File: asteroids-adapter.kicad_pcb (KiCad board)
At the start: 2 copper layers, 69 x 90.3 mm, 16 parts, among them J1 Asteroids PCB connector, J2 Asteroids harness connector, U1 TL074

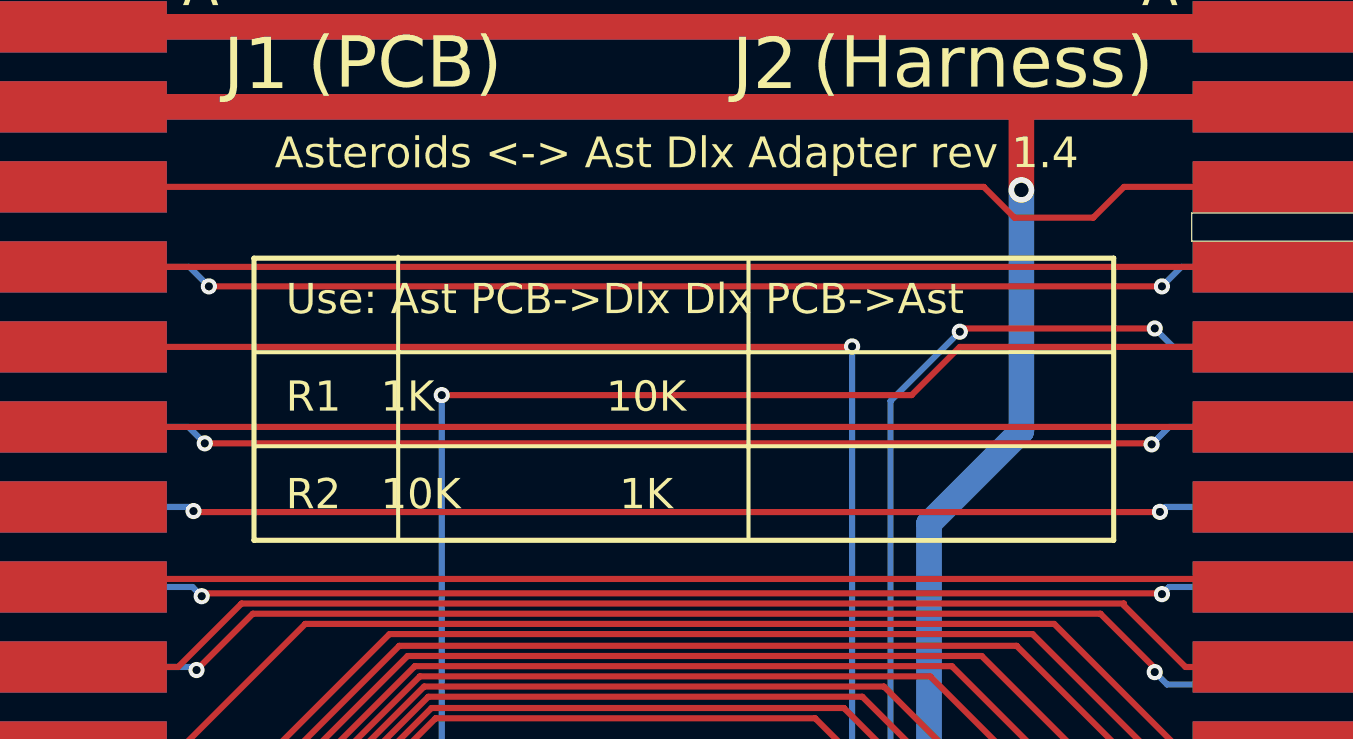
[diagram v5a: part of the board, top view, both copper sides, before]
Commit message: Rearranged config silk screen table
- easier to understand row format.
- white boxes to mark selected configuration.
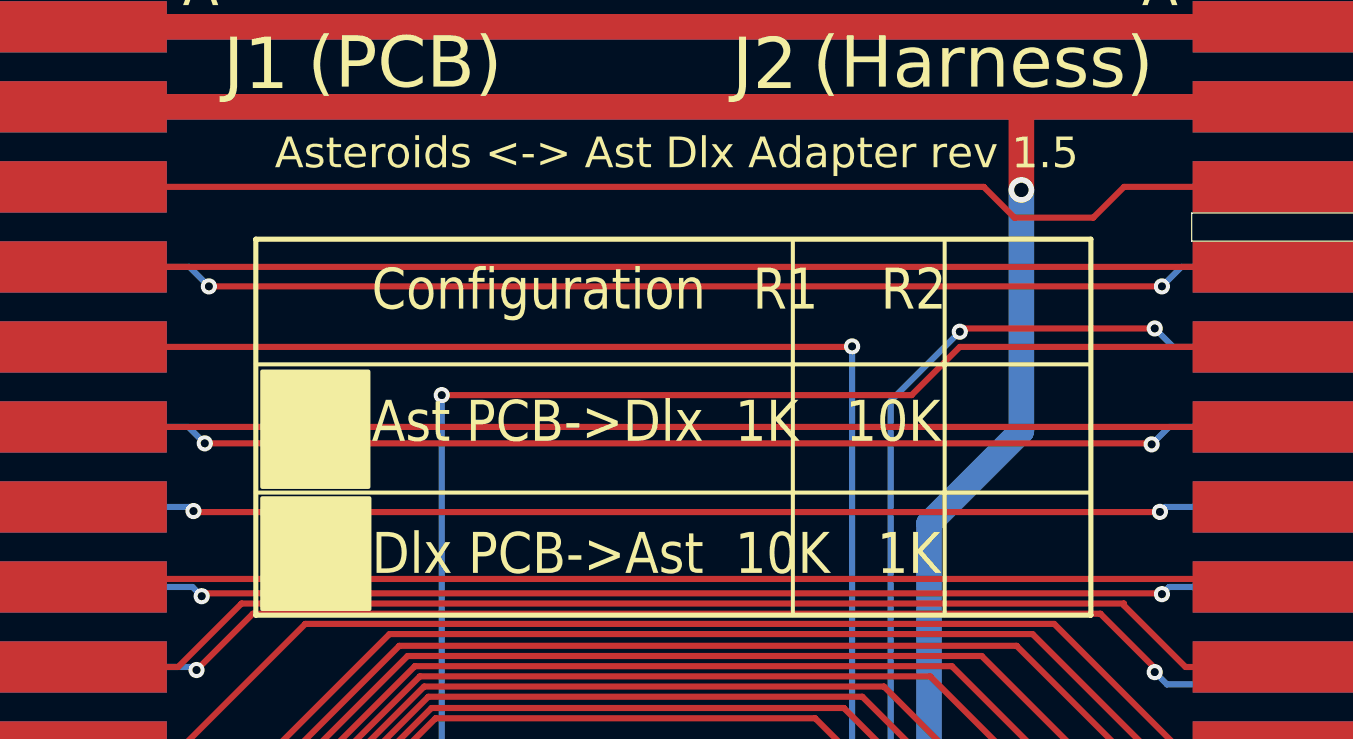
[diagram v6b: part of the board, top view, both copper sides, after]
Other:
- board text added: "Asteroids <-> Ast Dlx Adapter rev 1.5"
- board text added: "Configuration R1 R2 Ast PCB->Dlx 1K 10K Dlx PCB->Ast 10K 1K"
- board text removed: "Asteroids <-> Ast Dlx Adapter rev 1.4"
- board text removed: "Use: Ast PCB->Dlx Dlx PCB->Ast R1 1K 10K R2 10K 1K"
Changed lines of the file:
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@@
   (title_block
     (title "Asteroids to Asteroids Deluxe Adapter")
-    (date "2022-03-08")
-    (rev "1.4")
+    (date "2022-03-09")
+    (rev "1.5")
   )
   (layers
@@
     )
   )
-  (gr_line (start 145.2372 67.3862) (end 145.2372 81.3562) (layer "F.SilkS") (width 0.2))
-  (gr_line (start 120.7516 76.699532) (end 163.322 76.699532) (layer "F.SilkS") (width 0.2))
-  (gr_line (start 127.889 67.31) (end 127.889 81.28) (layer "F.SilkS") (width 0.2))
-  (gr_line (start 120.7516 72.042866) (end 163.322 72.042866) (layer "F.SilkS") (width 0.2))
-  (gr_rect (start 120.7516 67.3862) (end 163.322 81.3562) (layer "F.SilkS") (width 0.254) (fill none))
+  (gr_line (start 154.9527 66.4464) (end 154.9527 85.0646) (layer "F.SilkS") (width 0.2))
+  (gr_rect (start 121.158 78.7146) (end 126.4158 72.9996) (layer "F.SilkS") (width 0.2) (fill solid))
+  (gr_line (start 120.8405 78.994) (end 162.1917 78.994) (layer "F.SilkS") (width 0.2))
+  (gr_line (start 147.4343 66.4464) (end 147.4343 85.0646) (layer "F.SilkS") (width 0.2))
+  (gr_line (start 120.8405 72.644) (end 162.1917 72.644) (layer "F.SilkS") (width 0.2))
+  (gr_rect (start 121.158 84.7598) (end 126.4666 79.2734) (layer "F.SilkS") (width 0.2) (fill solid))
+  (gr_rect (start 120.8405 66.4464) (end 162.1917 85.0646) (layer "F.SilkS") (width 0.254) (fill none))
   (gr_poly
     (pts
@@
     (effects (font (size 1.905 1.905) (thickness 0.3)) (justify mirror))
   )
-  (gr_text "Asteroids <-> Ast Dlx Adapter rev 1.4" (at 141.6812 62.1792) (layer "F.SilkS")
+  (gr_text "Asteroids <-> Ast Dlx Adapter rev 1.5\n" (at 141.6812 62.1792) (layer "F.SilkS")
     (effects (font (size 1.524 1.524) (thickness 0.3)))
   )
@@
     (effects (font (size 1.905 1.905) (thickness 0.3)) (justify mirror))
   )
-  (gr_text "Use: Ast PCB->Dlx Dlx PCB->Ast\n\nR1   1K             10K\n \nR2   10K            1K" (at 122.3264 74.2442) (layer "F.SilkS")
-    (effects (font (size 1.5 1.5) (thickness 0.3)) (justify left))
+  (gr_text "Configuration   R1    R2\n\nAst PCB->Dlx  1K   10K\n\nDlx PCB->Ast  10K   1K" (at 126.5809 75.4888) (layer "F.SilkS")
+    (effects (font (size 2.032 1.778) (thickness 0.3048)) (justify left))
   )
   (segment (start 148.336 108.458) (end 138.43 108.458) (width 0.508) (layer "F.Cu") (net 1))
@@
     )
   )
-  (group "" (id 119bed15-d87d-4a81-bafe-b71226471a26)
+  (group "" (id 783ddcea-5963-4365-9c5b-b3f14c41286e)
     (members
       26e47b96-e9a5-48fa-bb2f-09aeb167fcf1
+      35b0aa54-b7ab-4dce-b263-08a43437121f
       644be4a6-1e55-414d-a68c-a545e48e63e7
       90662c63-00a8-414d-b291-156d808a5167
       d71882e2-ac98-42c6-8f8a-dd4c82632084
+      e6125ca4-8c3c-48b2-807d-2c2fe81d8bc7
       e79214a2-52a4-44d6-8e2b-47ef01e1d5a4
       eacccbd5-168c-4a45-b441-88af3d877755

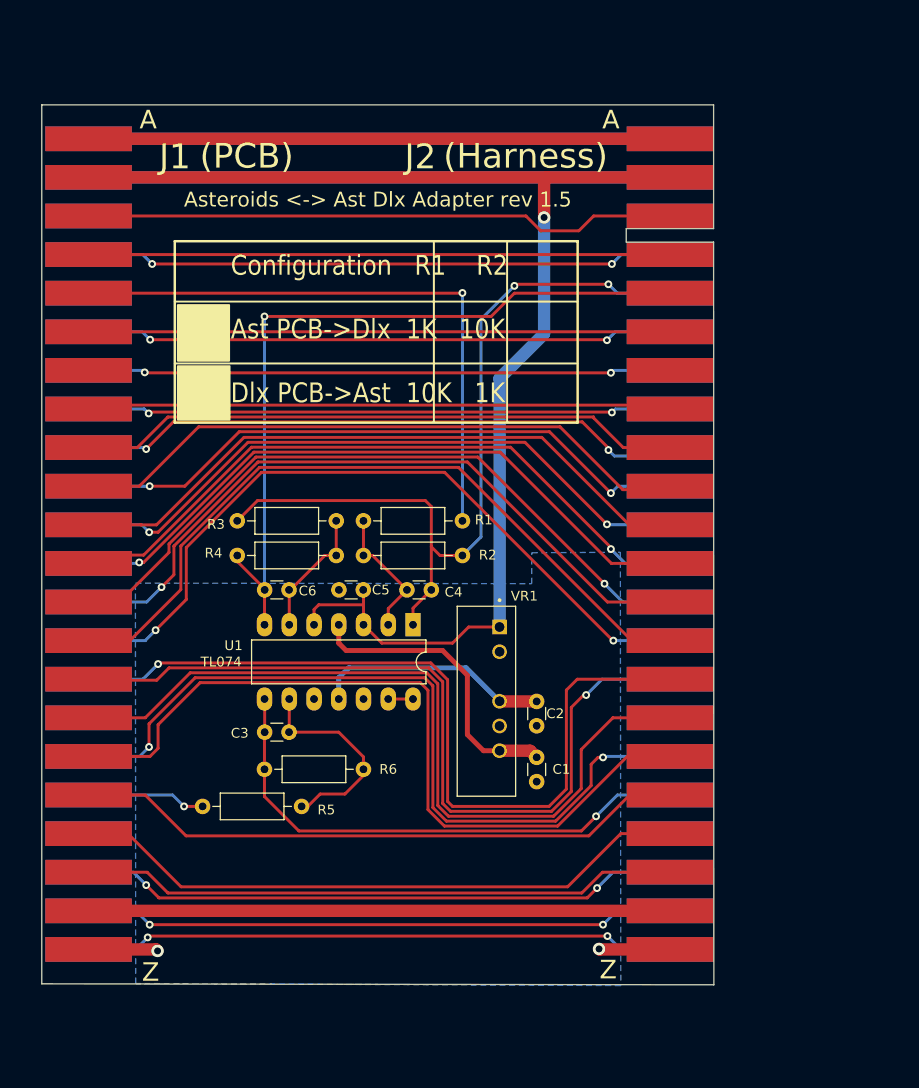
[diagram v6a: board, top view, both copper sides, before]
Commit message: Swith to PCB-mount edge connector
This is easier to assemble and provides a more reliable connection, due
to reduced likelyhood of distorting the edge connector position.
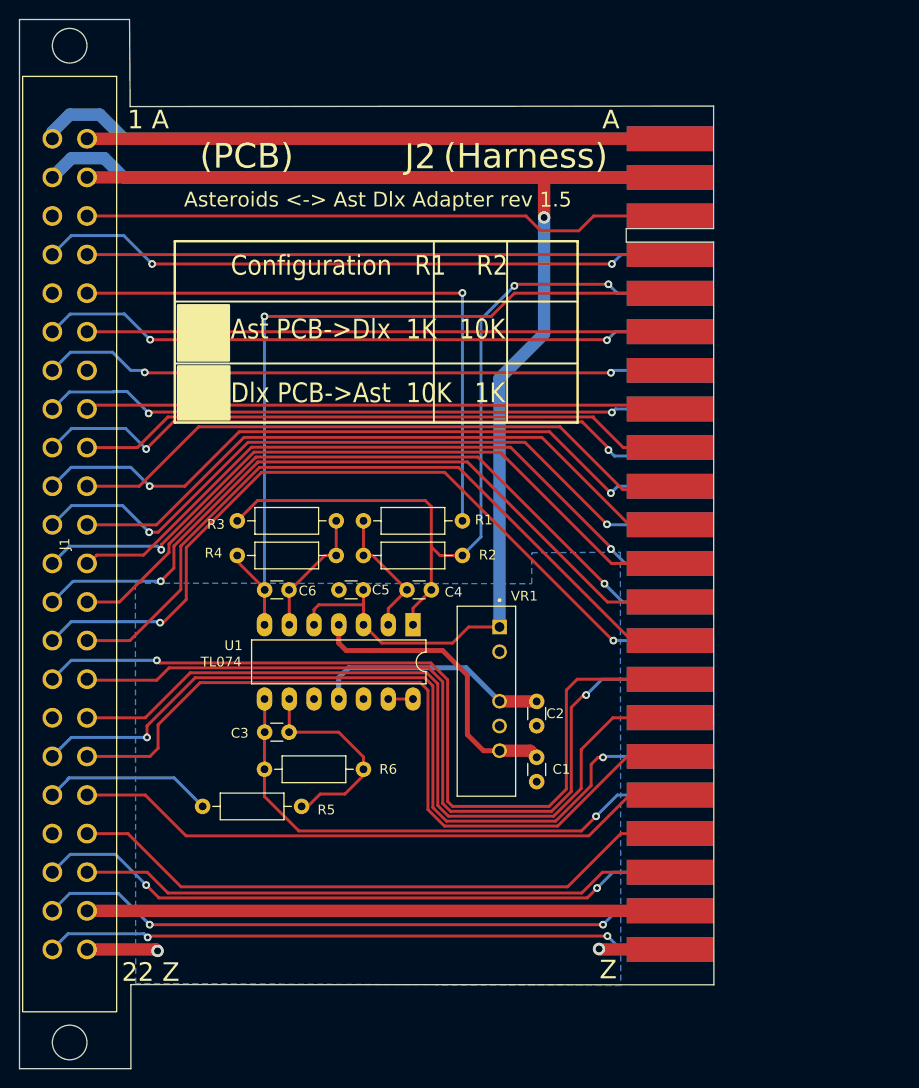
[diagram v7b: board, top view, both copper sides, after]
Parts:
- J1: footprint asteroids-adapter:edge 44-pin 0.156 inch -> asteroids-adapter:EDAC-305 44-pin edge 0.156
- moved J1 41.7 mm to (110.1, 97.5)
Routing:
- net Net-(J1-Pad1): track 59.7 -> 65.9 mm
- net Net-(J1-Pad11): track 67.3 -> 72.7 mm
- net Net-(J1-Pad2): track 59.7 -> 65.0 mm
- net Net-(J1-Pad4): track 60.5 -> 65.8 mm
- net Net-(J1-Pad10): track 64.9 -> 70.2 mm
- net Net-(J1-Pad9): track 62.8 -> 68.2 mm
- net Net-(J1-Pad7): track 59.9 -> 65.2 mm
- net Net-(J1-Pad20): track 61.9 -> 67.1 mm
- net Net-(J1-Pad8): track 60.1 -> 65.3 mm
- net Net-(J1-Pad6): track 60.4 -> 65.6 mm
- net Y_ORIG: track 12.2 -> 17.4 mm, vias 1 -> 0
- net Net-(J1-Pad21): track 60.9 -> 66.1 mm
- net START_1: track 69.2 -> 73.5 mm
- net Net-(J1-Pad22): track 60.8 -> 64.9 mm
- net ROT_RIGHT: track 85.2 -> 89.1 mm
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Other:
- board size 69 x 90.3 mm -> 71.3 x 107.7 mm
- board text added: "1 A"
- board text added: "22 Z"

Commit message: Added connections for X_INV and Y_INV
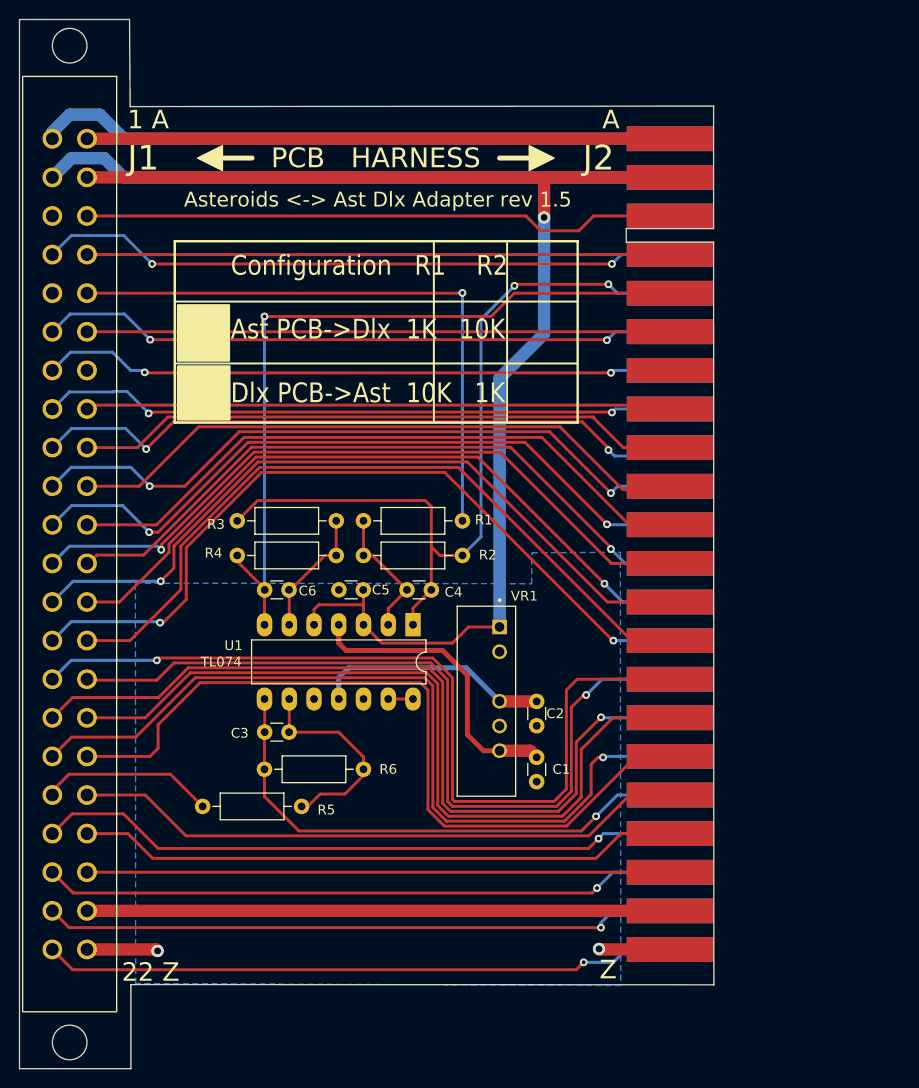
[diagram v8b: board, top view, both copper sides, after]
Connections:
- net Net-(J1-Pad2) renamed VCC
- net Net-(J1-PadY) renamed GND2
- J1 pad 16: unconnected-(J1-Pad16) -> Net-(J1-Pad16)
- J1 pad 19: unconnected-(J1-Pad19) -> Net-(J1-Pad19)
- J2 pad 16: unconnected-(J2-Pad16) -> Net-(J1-Pad16)
- J2 pad 19: unconnected-(J2-Pad19) -> Net-(J1-Pad19)
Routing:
- net Net-(J1-Pad16): track 0.00 -> 86.1 mm, vias 0 -> 1
- net Net-(J1-Pad19): track 0.00 -> 66.4 mm, vias 0 -> 1
- net Net-(J1-PadW): track 64.2 -> 61.8 mm
- net Net-(J1-Pad20): track 67.1 -> 65.2 mm, vias 2 -> 1
- net Net-(J1-PadX): track 61.5 -> 59.8 mm
- net Net-(J1-Pad21): track 66.1 -> 65.1 mm, vias 2 -> 1
- net Net-(J1-PadT): track 81.6 -> 82.1 mm
- net Y_ORIG: track 17.4 -> 17.9 mm
- net Net-(J1-Pad22): track 64.9 -> 65.1 mm, vias 2 -> 1
- net Net-(J1-Pad17): track 84.9 -> 84.7 mm, vias 2 -> 1
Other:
- board text added: "HARNESS PCB"
- board text added: "PCB HARNESS"
- board text removed: "(Harness)"
- board text removed: "(PCB)"
